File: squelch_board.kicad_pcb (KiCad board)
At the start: 2 copper layers, 50 x 50 mm, 91 parts, among them P1 PWR, P2 DISC., P3 OUT, P4 CONN_02X04, P5 CONN-10033526-N3212LF, P6 CONN_01X05, P7 LPF, P8 HPF, P9 DISC., U1 STM32F030F4P6, U2 Ricom R-786.5-0.5, U3 AP2202, U4 MCP6002, U5 MCP6002, U6 CP2105

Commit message: Renaming "HPF" to "NOISE" in schematic and on silk screen.
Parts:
- TP2: value HPF -> NOISE
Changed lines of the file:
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@@
       (effects (font (size 0.7 0.7) (thickness 0.127)))
     )
-    (fp_text value HPF (at -0.038013 3.154019) (layer F.SilkS)
+    (fp_text value NOISE (at -0.038013 3.154019) (layer F.SilkS)
       (effects (font (size 1.5 1.5) (thickness 0.3)))
     )

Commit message: Swapping out STM32F030F4P6 for STM32F070F6P
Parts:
- U1: value STM32F030F4P6 -> STM32F070F6P; footprint IPC7351-Nominal:SOP65P640X120-20 -> Package_SO:TSSOP-20_4.4x6.5mm_P0.65mm
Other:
- board text added: "(c) 2017, 2020, CC-BY-SA"
- board text removed: "(c) 2017, CC-BY-SA"
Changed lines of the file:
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@@
     (thickness 1.6)
     (drawings 105)
-    (tracks 599)
+    (tracks 598)
     (zones 0)
     (modules 91)
@@
   )
   (setup
-    (last_trace_width 0.5)
+    (last_trace_width 0.25)
     (user_trace_width 0.5)
     (user_trace_width 1)
@@
     (add_net "Net-(U6-Pad9)")
   )
+  (module Package_SO:TSSOP-20_4.4x6.5mm_P0.65mm (layer F.Cu)
+    (at 139.75 71.75 270)
+    (descr "20-Lead Plastic Thin Shrink Small Outline (ST)-4.4 mm Body [TSSOP] (see Microchip Packaging Specification 00000049BS.pdf)")
+    (tags "SSOP 0.65")
+    (attr smd)
+    (fp_text reference U1 (at 0 -4.3 90) (layer F.SilkS)
+      (effects (font (size 1 1) (thickness 0.15)))
+    )
+    (fp_text value STM32F070F6P (at 0 4.3 90) (layer F.Fab)
+      (effects (font (size 1 1) (thickness 0.15)))
+    )
+    (fp_text user %R (at 0 0 90) (layer F.Fab)
+      (effects (font (size 0.8 0.8) (thickness 0.15)))
+    )
+    (fp_line (start -3.75 -3.45) (end 2.225 -3.45) (layer F.SilkS) (width 0.15))
+    (fp_line (start -2.225 3.45) (end 2.225 3.45) (layer F.SilkS) (width 0.15))
+    (fp_line (start -3.95 3.55) (end 3.95 3.55) (layer F.CrtYd) (width 0.05))
+    (fp_line (start -3.95 -3.55) (end 3.95 -3.55) (layer F.CrtYd) (width 0.05))
+    (fp_line (start 3.95 -3.55) (end 3.95 3.55) (layer F.CrtYd) (width 0.05))
+    (fp_line (start -3.95 -3.55) (end -3.95 3.55) (layer F.CrtYd) (width 0.05))
+    (fp_line (start -2.2 -2.25) (end -1.2 -3.25) (layer F.Fab) (width 0.15))
+    (fp_line (start -2.2 3.25) (end -2.2 -2.25) (layer F.Fab) (width 0.15))
+    (fp_line (start 2.2 3.25) (end -2.2 3.25) (layer F.Fab) (width 0.15))
+    (fp_line (start 2.2 -3.25) (end 2.2 3.25) (layer F.Fab) (width 0.15))
+    (fp_line (start -1.2 -3.25) (end 2.2 -3.25) (layer F.Fab) (width 0.15))
+    (pad 20 smd rect (at 2.95 -2.925 270) (size 1.45 0.45) (layers F.Cu F.Paste F.Mask)
+      (net 23 "Net-(U1-Pad20)"))
+    (pad 19 smd rect (at 2.95 -2.275 270) (size 1.45 0.45) (layers F.Cu F.Paste F.Mask)
+      (net 22 "Net-(U1-Pad19)"))
+    (pad 18 smd rect (at 2.95 -1.625 270) (size 1.45 0.45) (layers F.Cu F.Paste F.Mask)
+      (net 37 /USB2uC))
+    (pad 17 smd rect (at 2.95 -0.975 270) (size 1.45 0.45) (layers F.Cu F.Paste F.Mask)
+      (net 36 /uC2USB))
+    (pad 16 smd rect (at 2.95 -0.325 270) (size 1.45 0.45) (layers F.Cu F.Paste F.Mask)
+      (net 2 /3V3))
+    (pad 15 smd rect (at 2.95 0.325 270) (size 1.45 0.45) (layers F.Cu F.Paste F.Mask)
+      (net 1 GND))
+    (pad 14 smd rect (at 2.95 0.975 270) (size 1.45 0.45) (layers F.Cu F.Paste F.Mask)
+      (net 21 "Net-(U1-Pad14)"))
+    (pad 13 smd rect (at 2.95 1.625 270) (size 1.45 0.45) (layers F.Cu F.Paste F.Mask)
+      (net 20 "Net-(U1-Pad13)"))
+    (pad 12 smd rect (at 2.95 2.275 270) (size 1.45 0.45) (layers F.Cu F.Paste F.Mask)
+      (net 19 "Net-(U1-Pad12)"))
+    (pad 11 smd rect (at 2.95 2.925 270) (size 1.45 0.45) (layers F.Cu F.Paste F.Mask)
+      (net 24 /LPF_OUT))
+    (pad 10 smd rect (at -2.95 2.925 270) (size 1.45 0.45) (layers F.Cu F.Paste F.Mask)
+      (net 49 /uC10))
+    (pad 9 smd rect (at -2.95 2.275 270) (size 1.45 0.45) (layers F.Cu F.Paste F.Mask)
+      (net 52 /uC9))
+    (pad 8 smd rect (at -2.95 1.625 270) (size 1.45 0.45) (layers F.Cu F.Paste F.Mask)
+      (net 54 /AF_MUTE))
+    (pad 7 smd rect (at -2.95 0.975 270) (size 1.45 0.45) (layers F.Cu F.Paste F.Mask)
+      (net 14 /AF_BUF))
+    (pad 6 smd rect (at -2.95 0.325 270) (size 1.45 0.45) (layers F.Cu F.Paste F.Mask)
+      (net 67 /NOISE))
+    (pad 5 smd rect (at -2.95 -0.325 270) (size 1.45 0.45) (layers F.Cu F.Paste F.Mask)
+      (net 2 /3V3))
+    (pad 4 smd rect (at -2.95 -0.975 270) (size 1.45 0.45) (layers F.Cu F.Paste F.Mask)
+      (net 38 /~RST))
+    (pad 3 smd rect (at -2.95 -1.625 270) (size 1.45 0.45) (layers F.Cu F.Paste F.Mask)
+      (net 51 /uC3))
+    (pad 2 smd rect (at -2.95 -2.275 270) (size 1.45 0.45) (layers F.Cu F.Paste F.Mask)
+      (net 50 /uC2))
+    (pad 1 smd rect (at -2.95 -2.925 270) (size 1.45 0.45) (layers F.Cu F.Paste F.Mask)
+      (net 39 /BOOT0))
+    (model ${KISYS3DMOD}/Package_SO.3dshapes/TSSOP-20_4.4x6.5mm_P0.65mm.wrl
+      (at (xyz 0 0 0))
+      (scale (xyz 1 1 1))
+      (rotate (xyz 0 0 0))
+    )
+  )
   (module local:R-78xx-0.5 (layer B.Cu)
     (at 120.946928 75.037967 180)
@@
     )
   )
-  (module IPC7351-Nominal:SOP65P640X120-20 (layer F.Cu)
-    (at 139.75 71.75 270)
-    (descr "SOP,0.65mm pitch;20 pin,4.50mm W X 6.60mm L X 1.20mm H Body")
-    (attr smd)
-    (fp_text reference U1 (at 2 -4.25 90) (layer F.SilkS)
-      (effects (font (size 0.7 0.7) (thickness 0.127)))
-    )
-    (fp_text value STM32F030F4P6 (at 0 0 270) (layer F.Fab)
-      (effects (font (size 0.5 0.5) (thickness 0.1)))
-    )
-    (fp_line (start -2.25 -3.404) (end -2.25 -3.427) (layer F.SilkS) (width 0.15))
-    (fp_line (start -2.25 -3.427) (end 2.25 -3.427) (layer F.SilkS) (width 0.15))
-    (fp_line (start 2.25 -3.427) (end 2.25 -3.404) (layer F.SilkS) (width 0.15))
-    (fp_line (start -2.25 3.404) (end -2.25 3.427) (layer F.SilkS) (width 0.15))
-    (fp_line (start -2.25 3.427) (end 2.25 3.427) (layer F.SilkS) (width 0.15))
-    (fp_line (start 2.25 3.427) (end 2.25 3.404) (layer F.SilkS) (width 0.15))
-    (fp_line (start -2.885 -3.658) (end -2.758 -3.785) (layer F.SilkS) (width 0.15))
-    (fp_line (start -2.758 -3.785) (end -2.631 -3.658) (layer F.SilkS) (width 0.15))
-    (fp_line (start -2.631 -3.658) (end -2.758 -3.531) (layer F.SilkS) (width 0.15))
-    (fp_line (start -2.758 -3.531) (end -2.885 -3.658) (layer F.SilkS) (width 0.15))
-    (fp_line (start -3.925 -4.035) (end 3.925 -4.035) (layer F.CrtYd) (width 0.05))
-    (fp_line (start 3.925 -4.035) (end 3.925 3.677) (layer F.CrtYd) (width 0.05))
-    (fp_line (start 3.925 3.677) (end -3.925 3.677) (layer F.CrtYd) (width 0.05))
-    (fp_line (start -3.925 3.677) (end -3.925 -4.035) (layer F.CrtYd) (width 0.05))
-    (pad 1 smd oval (at -2.95 -2.925 270) (size 1.45 0.45) (layers F.Cu F.Paste F.Mask)
-      (net 39 /BOOT0))
-    (pad 2 smd oval (at -2.95 -2.275 270) (size 1.45 0.45) (layers F.Cu F.Paste F.Mask)
-      (net 50 /uC2))
-    (pad 3 smd oval (at -2.95 -1.625 270) (size 1.45 0.45) (layers F.Cu F.Paste F.Mask)
-      (net 51 /uC3))
-    (pad 4 smd oval (at -2.95 -0.975 270) (size 1.45 0.45) (layers F.Cu F.Paste F.Mask)
-      (net 38 /~RST))
-    (pad 5 smd oval (at -2.95 -0.325 270) (size 1.45 0.45) (layers F.Cu F.Paste F.Mask)
-      (net 2 /3V3))
-    (pad 6 smd oval (at -2.95 0.325 270) (size 1.45 0.45) (layers F.Cu F.Paste F.Mask)
-      (net 67 /NOISE))
-    (pad 7 smd oval (at -2.95 0.975 270) (size 1.45 0.45) (layers F.Cu F.Paste F.Mask)
-      (net 14 /AF_BUF))
-    (pad 8 smd oval (at -2.95 1.625 270) (size 1.45 0.45) (layers F.Cu F.Paste F.Mask)
-      (net 54 /AF_MUTE))
-    (pad 9 smd oval (at -2.95 2.275 270) (size 1.45 0.45) (layers F.Cu F.Paste F.Mask)
-      (net 52 /uC9))
-    (pad 10 smd oval (at -2.95 2.925 270) (size 1.45 0.45) (layers F.Cu F.Paste F.Mask)
-      (net 49 /uC10))
-    (pad 11 smd oval (at 2.95 2.925 270) (size 1.45 0.45) (layers F.Cu F.Paste F.Mask)
-      (net 24 /LPF_OUT))
-    (pad 12 smd oval (at 2.95 2.275 270) (size 1.45 0.45) (layers F.Cu F.Paste F.Mask)
-      (net 19 "Net-(U1-Pad12)"))
-    (pad 13 smd oval (at 2.95 1.625 270) (size 1.45 0.45) (layers F.Cu F.Paste F.Mask)
-      (net 20 "Net-(U1-Pad13)"))
-    (pad 14 smd oval (at 2.95 0.975 270) (size 1.45 0.45) (layers F.Cu F.Paste F.Mask)
-      (net 21 "Net-(U1-Pad14)"))
-    (pad 15 smd oval (at 2.95 0.325 270) (size 1.45 0.45) (layers F.Cu F.Paste F.Mask)
-      (net 1 GND))
-    (pad 16 smd oval (at 2.95 -0.325 270) (size 1.45 0.45) (layers F.Cu F.Paste F.Mask)
-      (net 2 /3V3))
-    (pad 17 smd oval (at 2.95 -0.975 270) (size 1.45 0.45) (layers F.Cu F.Paste F.Mask)
-      (net 36 /uC2USB))
-    (pad 18 smd oval (at 2.95 -1.625 270) (size 1.45 0.45) (layers F.Cu F.Paste F.Mask)
-      (net 37 /USB2uC))
-    (pad 19 smd oval (at 2.95 -2.275 270) (size 1.45 0.45) (layers F.Cu F.Paste F.Mask)
-      (net 22 "Net-(U1-Pad19)"))
-    (pad 20 smd oval (at 2.95 -2.925 270) (size 1.45 0.45) (layers F.Cu F.Paste F.Mask)
-      (net 23 "Net-(U1-Pad20)"))
-    (model smd_dil/tssop-20.wrl
-      (at (xyz 0 0 0))
-      (scale (xyz 1 1 1))
-      (rotate (xyz 0 0 90))
-    )
-  )
   (module Capacitors_SMD:C_0603 (layer F.Cu)
     (at 153 68.5 90)
@@
   )
   (gr_line (start 136.75 82) (end 133.25 82) (layer B.SilkS) (width 0.2))
-  (gr_text "(c) 2017, CC-BY-SA" (at 163.5 88.7 90) (layer F.SilkS)
+  (gr_text "(c) 2017, 2020, CC-BY-SA" (at 163.5 88.7 90) (layer F.SilkS)
     (effects (font (size 0.75 0.75) (thickness 0.15)))
   )
@@
   (segment (start 141.5 73.25) (end 143.732339 75.482339) (width 0.5) (layer B.Cu) (net 38))
   (segment (start 143.732339 75.482339) (end 151.25 75.482339) (width 0.5) (layer B.Cu) (net 38))
-  (segment (start 140.725 69.475) (end 141.5 70.25) (width 0.25) (layer F.Cu) (net 38))
-  (segment (start 141.5 70.25) (end 141.5 70.5) (width 0.25) (layer F.Cu) (net 38))
-  (segment (start 140.725 68.8) (end 140.725 69.475) (width 0.25) (layer F.Cu) (net 38))
   (segment (start 157.25 76.25) (end 160.75 79.75) (width 0.5) (layer F.Cu) (net 38))
   (segment (start 160.75 79.75) (end 160.75 83.59) (width 0.5) (layer F.Cu) (net 38))
@@
   (segment (start 150 74.8) (end 150 75.3) (width 0.25) (layer F.Cu) (net 38))
   (segment (start 150 75.3) (end 150.2 75.5) (width 0.25) (layer F.Cu) (net 38))
+  (segment (start 140.725 69.725) (end 141.5 70.5) (width 0.25) (layer F.Cu) (net 38))
+  (segment (start 140.725 68.8) (end 140.725 69.725) (width 0.25) (layer F.Cu) (net 38))
   (segment (start 142.675 69.425) (end 143.75 70.5) (width 0.25) (layer F.Cu) (net 39))
   (segment (start 143.75 70.5) (end 144.5 70.5) (width 0.25) (layer F.Cu) (net 39))

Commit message: Slight rearrangement of schematic, renaming nodes for consistency.
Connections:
- net /AF_BUF renamed /AF
- net /AF_MUTE renamed /MUTE
- net /LPF_OUT renamed /LPF

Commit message: Bumping version number to 2.0
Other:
- board text added: "HB9UF Squelch Board Rev 2.0 Design by Matt Weyland, HB9FRV"
- board text removed: "HB9UF Squelch Board Rev 1.3 Design by Matt Weyland, HB9FRV PCB supplied by Hackvana"

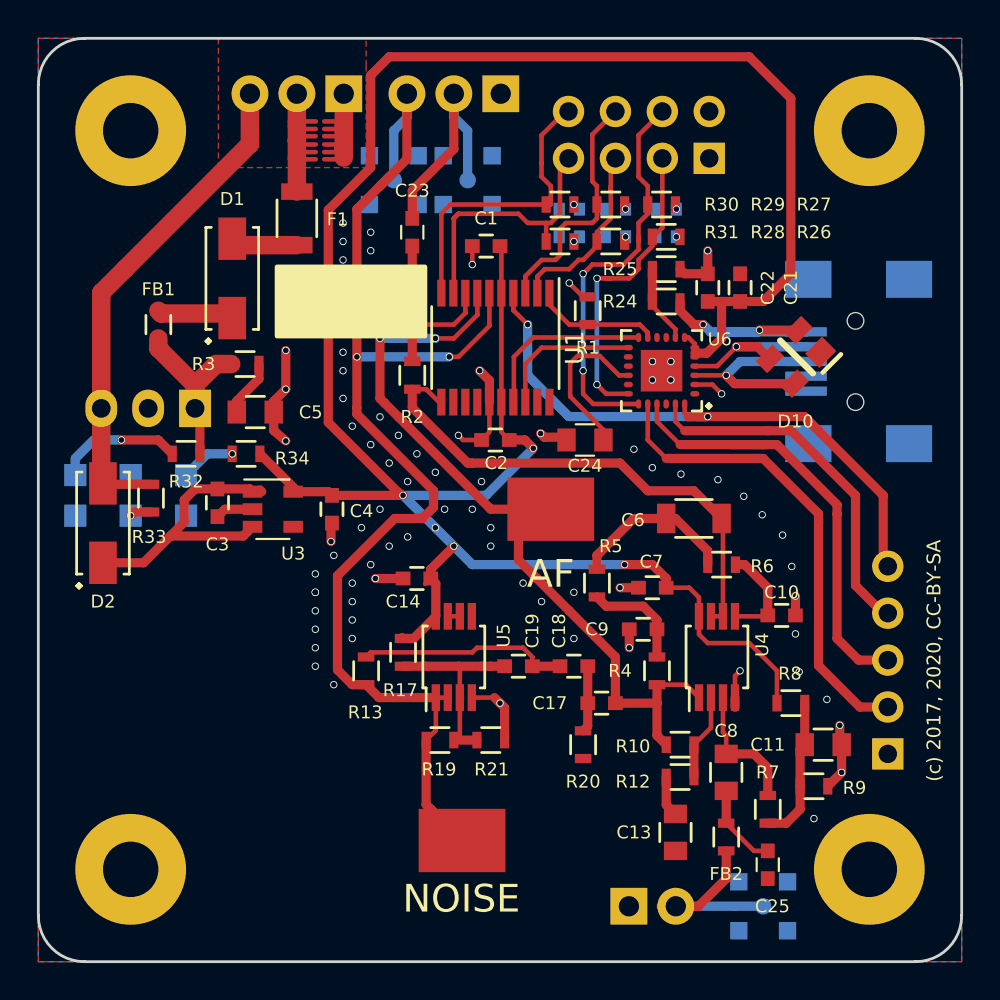
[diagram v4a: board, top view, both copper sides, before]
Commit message: Swapping out footprints for current ones in order to have 3d models
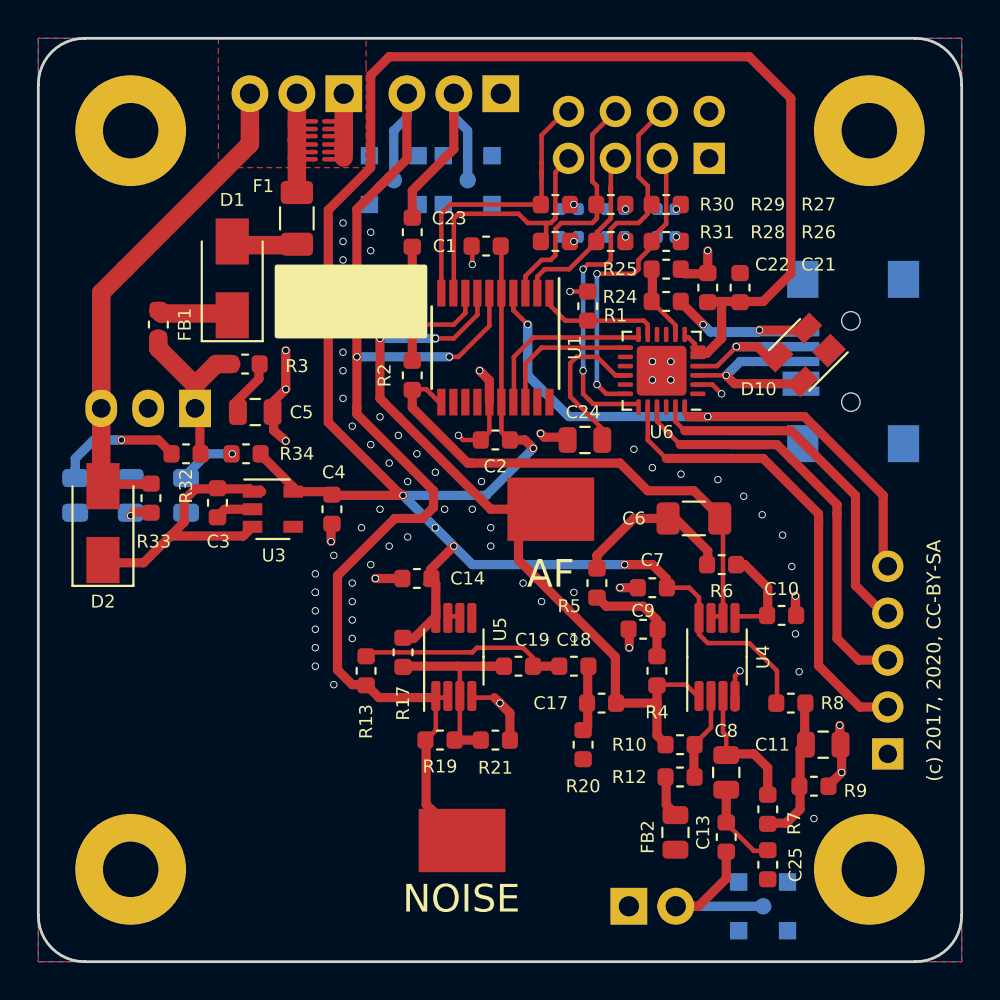
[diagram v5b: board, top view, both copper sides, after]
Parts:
- C1, C10, C14, C17, C18, C19, C2, C21, C22, C23, C25, C3, C4, C7, C9: footprint Capacitors_SMD:C_0603 -> Capacitor_SMD:C_0603_1608Metric
- C11, C13, C24, C5, C8: footprint Capacitors_SMD:C_0805 -> Capacitor_SMD:C_0805_2012Metric
- C6: footprint Capacitors_SMD:C_1206 -> Capacitor_SMD:C_1206_3216Metric
- D1, D2: footprint IPC7351-Nominal:DIOM5326X292 -> Diode_SMD:D_SMA
- D10: footprint smd-semi:SOT-143 -> Package_TO_SOT_SMD:SOT-143
- D11, D12, D13: footprint LEDs:LED_0805 -> LED_SMD:LED_0805_2012Metric
- D4, D5, D6, D7, D8, D9: footprint LEDs:LED_0402 -> LED_SMD:LED_0402_1005Metric
- F1: footprint Resistors_SMD:R_1206 -> Resistor_SMD:R_1206_3216Metric
- FB1, FB2, R1, R10, R12, R13, R17, R19, R2, R20, R21, R24, R25, R26, R27, R28, R29, R3, R30, R31, R32, R33, R34, R4, R5, R6, R7, R8, R9: footprint Resistors_SMD:R_0603 -> Resistor_SMD:R_0603_1608Metric
- MP1, MP2, MP3, MP4: footprint MountingHole_3mm_Pad -> MountingHole:MountingHole_3mm_Pad
- P4: footprint Pin_Headers:Pin_Header_Angled_2x04_Pitch2.54mm -> Connector_PinHeader_2.54mm:PinHeader_2x04_P2.54mm_Horizontal
- P5: footprint conn-fci:CONN-10033526-N3212LF -> Connector_USB:USB_Mini-B_Lumberg_2486_01_Horizontal
- P6: footprint Pin_Headers:Pin_Header_Angled_1x05_Pitch2.54mm -> Connector_PinHeader_2.54mm:PinHeader_1x05_P2.54mm_Horizontal
- U3: footprint TO_SOT_Packages_SMD:SOT-23-5 -> Package_TO_SOT_SMD:SOT-23-5
- U4, U5: footprint Housings_SSOP:MSOP-8_3x3mm_Pitch0.65mm -> Package_SO:MSOP-8_3x3mm_P0.65mm
- U6: footprint IPC7351-Nominal:PQFN50P400X400X100-25 -> Package_DFN_QFN:QFN-24-1EP_4x4mm_P0.5mm_EP2.7x2.7mm
- moved D10 0.45 mm to (156.5, 72.1)
- moved P5 0.25 mm to (159.0, 72.5)
- moved R1 0.25 mm to (144.8, 69.5)
- moved R21 0.25 mm to (139.8, 93.0)
- moved R26 0.25 mm to (149.0, 66.0)
- moved R27 0.25 mm to (149.0, 64.0)
- moved R30 0.25 mm to (143.0, 64.0)
- moved R31 0.25 mm to (143.0, 66.0)
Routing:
- net Net-(R24-Pad1): track 4.22 -> 4.77 mm
- net GND: vias 86 -> 85

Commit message: Adding HB9UF artwork on backside of PCB
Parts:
- added G***: LOGO, symbols:hb9uf_logo_tiny, F.Cu at (126.8, 90.5)
- moved TP2 2.20 mm to (135.8, 98.4)
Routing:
- net /NOISE: track 71.0 -> 67.9 mm
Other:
- board text added: "HB9UF"
- board text added: "HB9UHF"

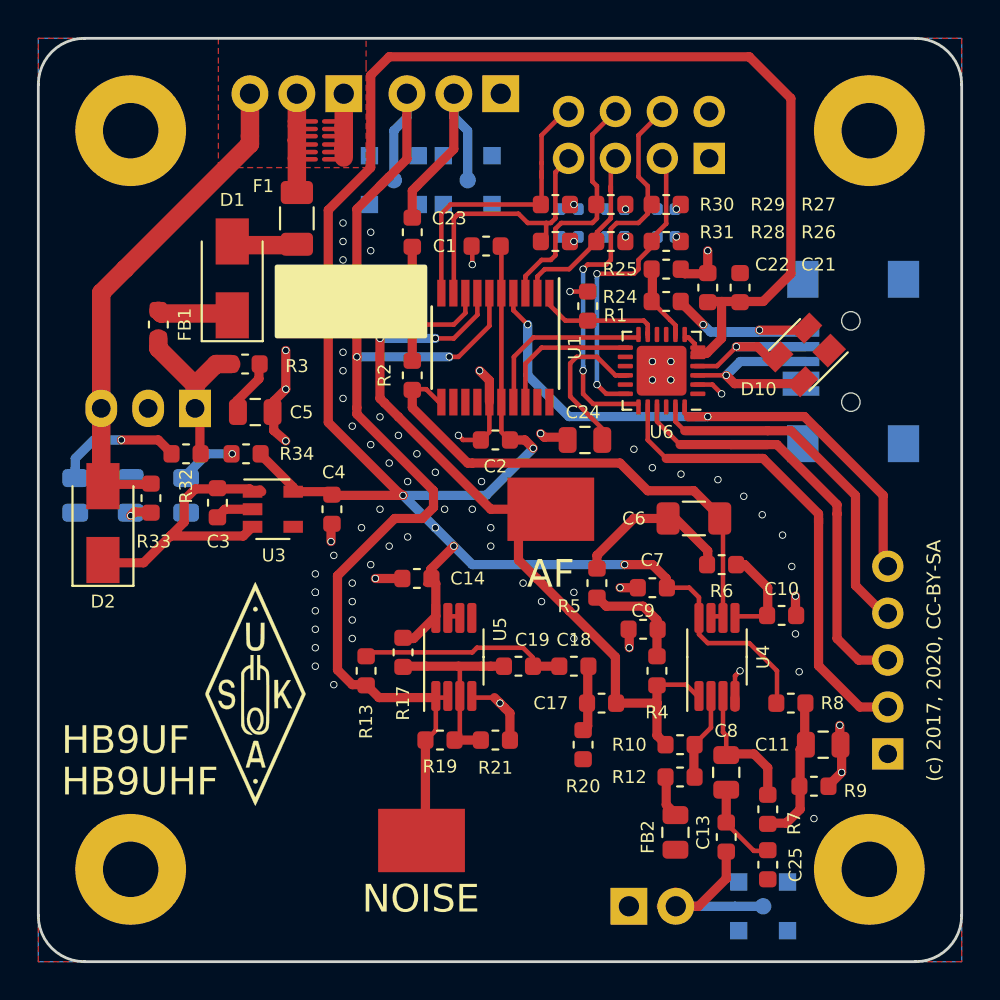
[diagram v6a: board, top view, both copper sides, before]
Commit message: Moving testpoints to board edge
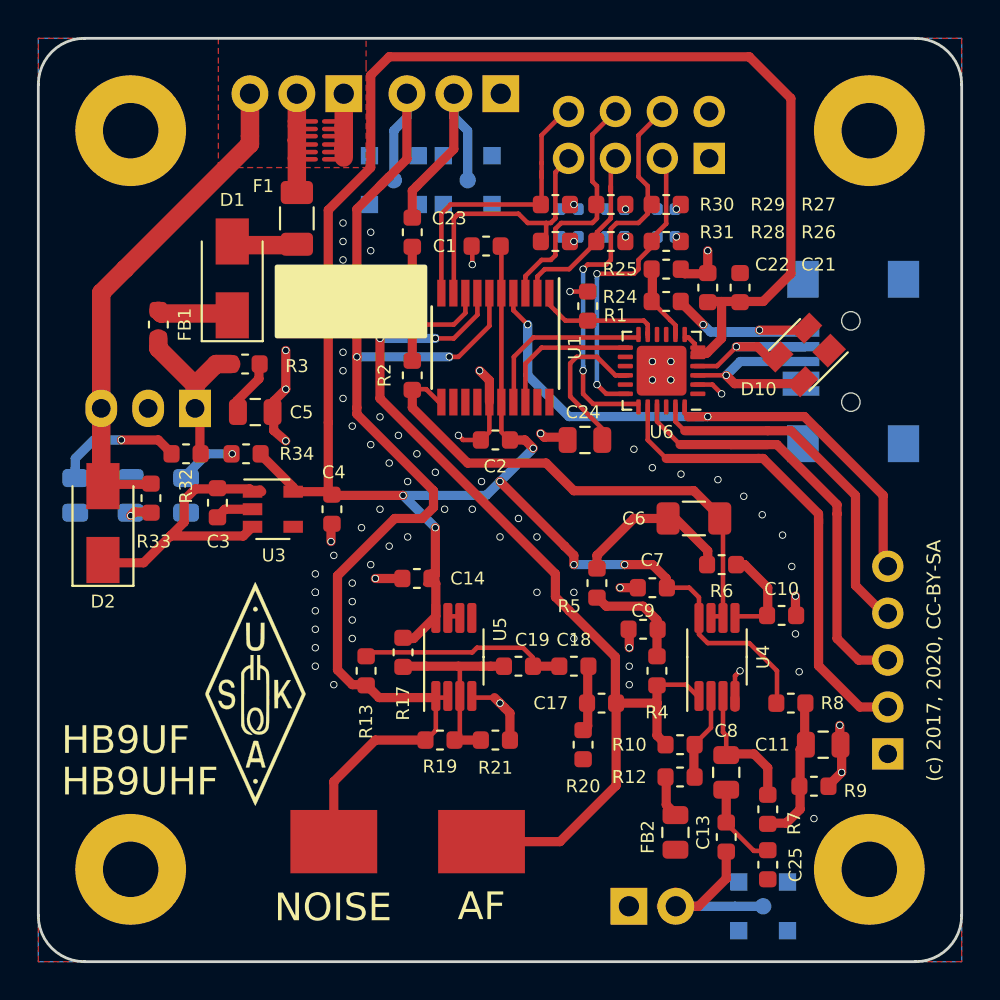
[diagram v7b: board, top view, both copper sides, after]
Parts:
- moved TP1 18.4 mm to (139.0, 98.5)
- moved TP2 4.75 mm to (131.0, 98.5)
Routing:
- net /AF: track 41.7 -> 53.3 mm
- net /NOISE: track 67.9 -> 71.4 mm
- net /3V3: track 133.2 -> 130.0 mm, vias 5 -> 6
- net GND: vias 85 -> 87
